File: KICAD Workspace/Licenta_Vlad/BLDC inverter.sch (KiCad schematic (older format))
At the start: 0 parts

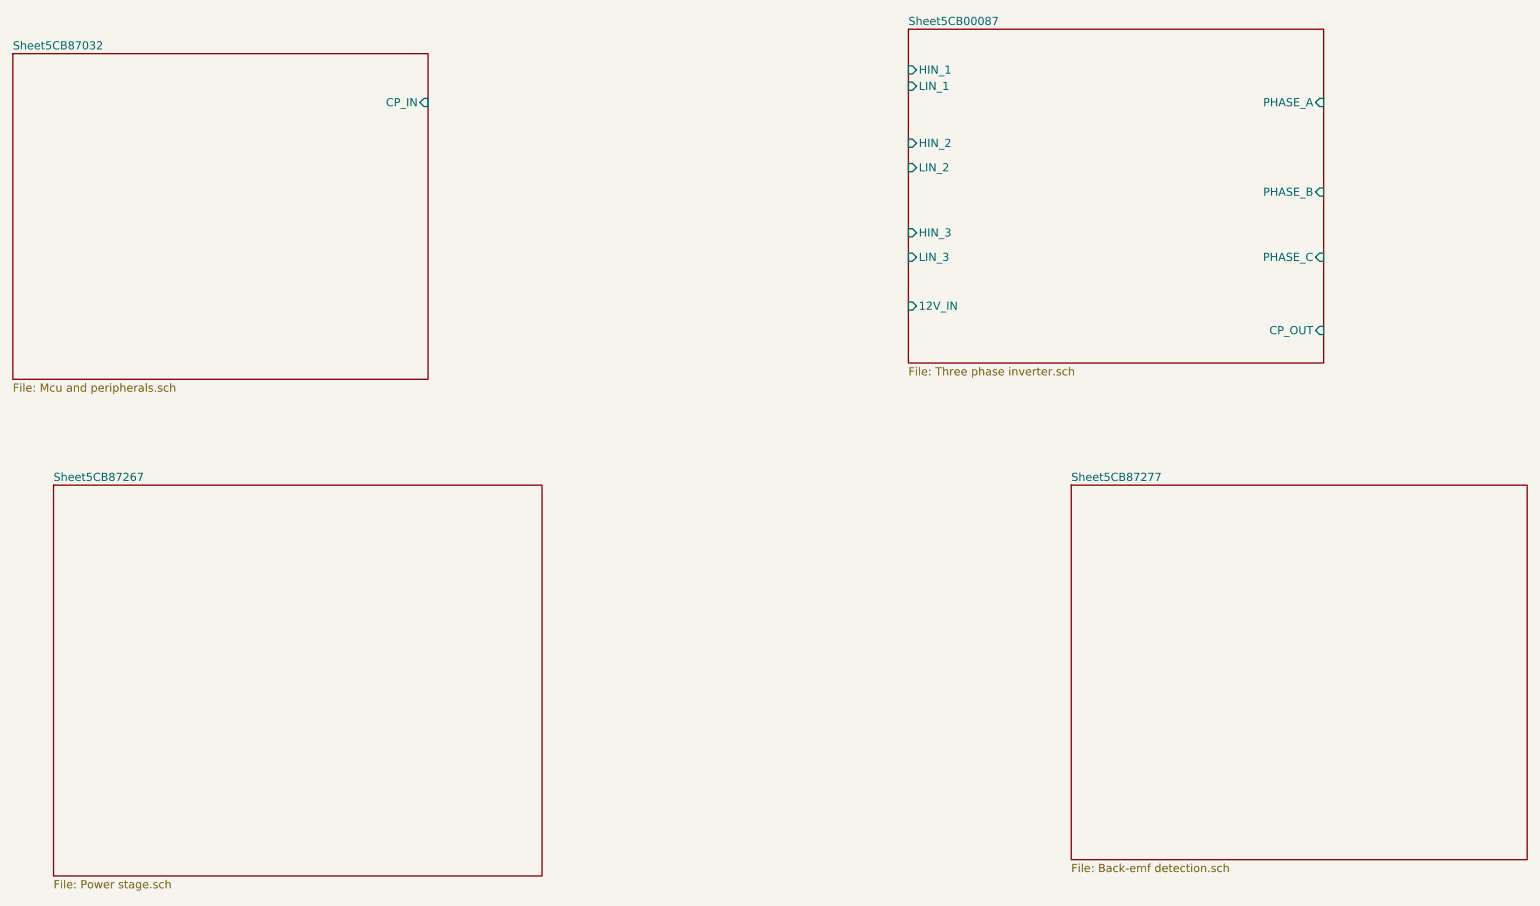
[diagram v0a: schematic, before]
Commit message: Added schematic for BEMF.
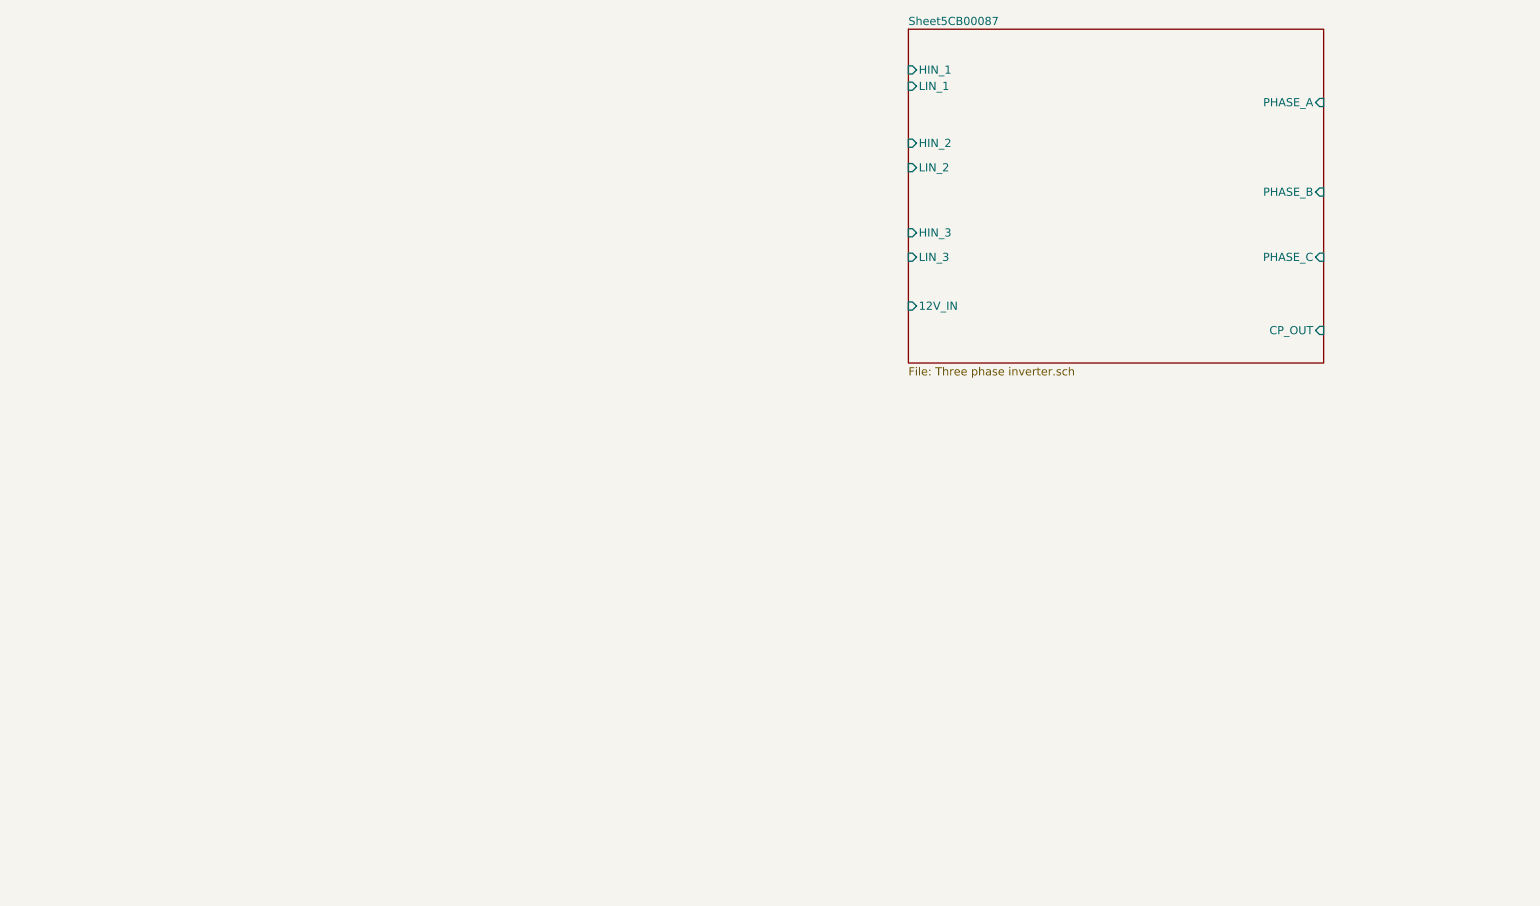
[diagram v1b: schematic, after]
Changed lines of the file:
@@
 EESchema Schematic File Version 4
+LIBS:BLDC inverter-cache
 EELAYER 26 0
 EELAYER END
 $Descr User 11811 8661
 encoding utf-8
-Sheet 1 5
+Sheet 1 2
 Title ""
 Date ""
@@
 F12 "CP_OUT" I R 8850 2900 50
 $EndSheet
-$Sheet
-S 800  1200 2550 2000
-U 5CB87033
-F0 "Sheet5CB87032" 50
-F1 "Mcu and peripherals.sch" 50
-F2 "CP_IN" I R 3350 1500 50
-$EndSheet
-$Sheet
-S 1050 3850 3000 2400
-U 5CB87268
-F0 "Sheet5CB87267" 50
-F1 "Power stage.sch" 50
-$EndSheet
-$Sheet
-S 7300 3850 2800 2300
-U 5CB87278
-F0 "Sheet5CB87277" 50
-F1 "Back-emf detection.sch" 50
-$EndSheet
 $EndSCHEMATC
